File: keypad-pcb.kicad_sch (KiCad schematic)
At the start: 34 parts, among them J1 AVR-ISP-6, SW1 SW_Push, SW2 SW_Push, SW3 SW_Push, SW4 SW_Push, SW5 SW_Push, SW6 SW_Push, U1 ATmega32U4-A, Y1 Crystal_GND24_Small

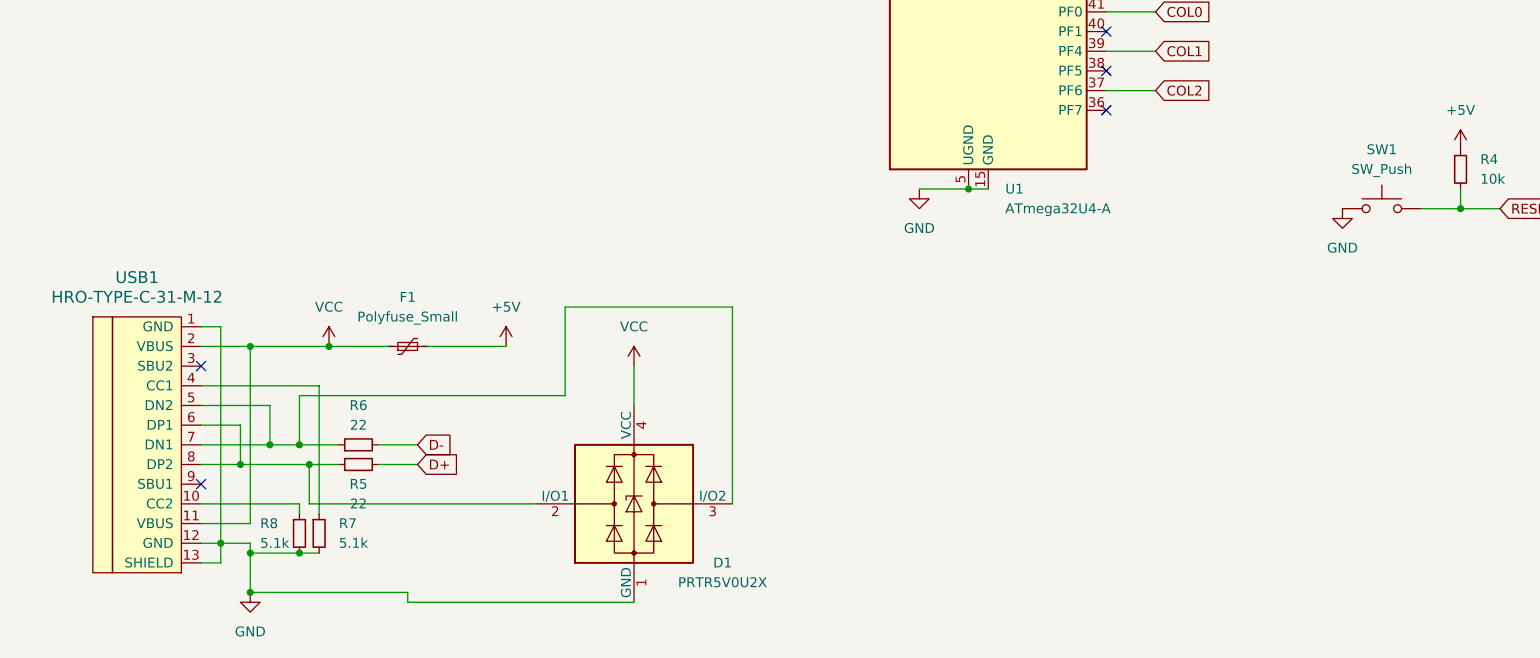
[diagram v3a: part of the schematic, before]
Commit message: power flag
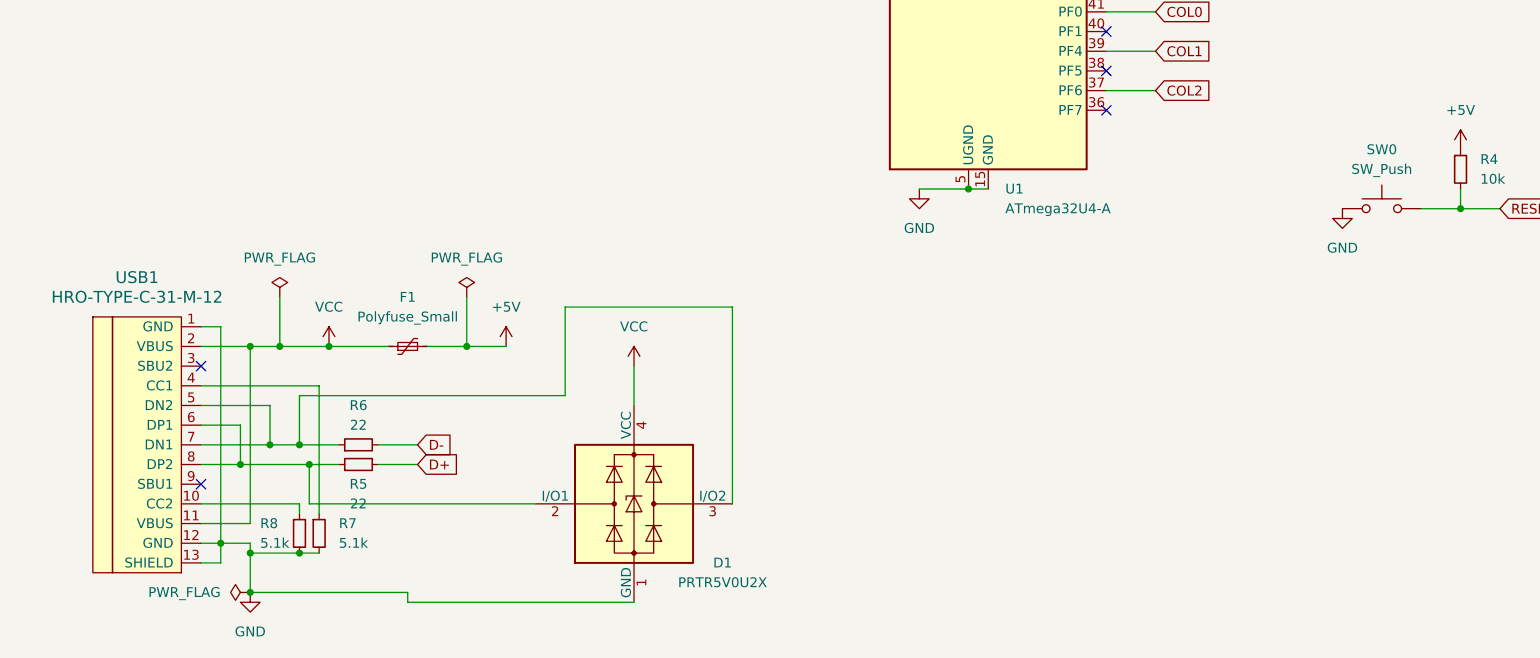
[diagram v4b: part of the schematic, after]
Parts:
- renumbered SW1 to SW0
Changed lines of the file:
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@@
   (junction (at 82.55 96.52) (diameter 0) (color 0 0 0 0)
   )
+  (junction (at 49.53 158.75) (diameter 0) (color 0 0 0 0)
+  )
   (junction (at 140.97 46.99) (diameter 0) (color 0 0 0 0)
   )
@@
   )
   (junction (at 73.66 91.44) (diameter 0) (color 0 0 0 0)
+  )
+  (junction (at 73.66 158.75) (diameter 0) (color 0 0 0 0)
   )
   (junction (at 52.07 171.45) (diameter 0) (color 0 0 0 0)
@@
     (stroke (width 0) (type default))
   )
-  (wire (pts (xy 68.58 158.75) (xy 78.74 158.75))
+  (wire (pts (xy 68.58 158.75) (xy 73.66 158.75))
     (stroke (width 0) (type default))
   )
@@
     (stroke (width 0) (type default))
   )
+  (wire (pts (xy 49.53 152.4) (xy 49.53 158.75))
+    (stroke (width 0) (type default))
+  )
   (wire (pts (xy 66.04 190.5) (xy 45.72 190.5))
     (stroke (width 0) (type default))
@@
     (stroke (width 0) (type default))
   )
+  (wire (pts (xy 49.53 158.75) (xy 55.88 158.75))
+    (stroke (width 0) (type default))
+  )
   (wire (pts (xy 52.07 185.42) (xy 54.61 185.42))
     (stroke (width 0) (type default))
@@
     (stroke (width 0) (type default))
   )
+  (wire (pts (xy 73.66 152.4) (xy 73.66 158.75))
+    (stroke (width 0) (type default))
+  )
   (wire (pts (xy 41.91 184.15) (xy 45.72 184.15))
     (stroke (width 0) (type default))
@@
     (stroke (width 0) (type default))
   )
-  (wire (pts (xy 45.72 158.75) (xy 55.88 158.75))
+  (wire (pts (xy 45.72 158.75) (xy 49.53 158.75))
     (stroke (width 0) (type default))
   )
@@
   )
   (wire (pts (xy 119.38 82.55) (xy 125.73 82.55))
+    (stroke (width 0) (type default))
+  )
+  (wire (pts (xy 73.66 158.75) (xy 78.74 158.75))
     (stroke (width 0) (type default))
   )
@@
     )
   )
+  (symbol (lib_id "power:PWR_FLAG") (at 45.72 190.5 90) (unit 1)
+    (in_bom yes) (on_board yes) (dnp no) (fields_autoplaced)
+    (property "Reference" "#FLG03" (at 43.815 190.5 0)
+      (effects (font (size 1.27 1.27)) hide)
+    )
+    (property "Value" "PWR_FLAG" (at 41.91 190.5 90)
+      (effects (font (size 1.27 1.27)) (justify left))
+    )
+    (property "Footprint" "" (at 45.72 190.5 0)
+      (effects (font (size 1.27 1.27)) hide)
+    )
+    (property "Datasheet" "~" (at 45.72 190.5 0)
+      (effects (font (size 1.27 1.27)) hide)
+    )
+    (pin "1")
+    (instances
+      (project "keypad-pcb"
+        (path "/73f1bcf6-a3cb-4955-8c73-ee07117345ce"
+          (reference "#FLG03") (unit 1)
+        )
+      )
+    )
+  )
   (symbol (lib_id "Device:C_Small") (at 64.77 93.98 0) (unit 1)
     (in_bom yes) (on_board yes) (dnp no) (fields_autoplaced)
@@
         (path "/73f1bcf6-a3cb-4955-8c73-ee07117345ce"
           (reference "#PWR012") (unit 1)
+        )
+      )
+    )
+  )
+  (symbol (lib_id "power:PWR_FLAG") (at 49.53 152.4 0) (unit 1)
+    (in_bom yes) (on_board yes) (dnp no) (fields_autoplaced)
+    (property "Reference" "#FLG01" (at 49.53 150.495 0)
+      (effects (font (size 1.27 1.27)) hide)
+    )
+    (property "Value" "PWR_FLAG" (at 49.53 147.32 0)
+      (effects (font (size 1.27 1.27)))
+    )
+    (property "Footprint" "" (at 49.53 152.4 0)
+      (effects (font (size 1.27 1.27)) hide)
+    )
+    (property "Datasheet" "~" (at 49.53 152.4 0)
+      (effects (font (size 1.27 1.27)) hide)
+    )
+    (pin "1")
+    (instances
+      (project "keypad-pcb"
+        (path "/73f1bcf6-a3cb-4955-8c73-ee07117345ce"
+          (reference "#FLG01") (unit 1)
+        )
+      )
+    )
+  )
+  (symbol (lib_id "power:PWR_FLAG") (at 73.66 152.4 0) (unit 1)
+    (in_bom yes) (on_board yes) (dnp no) (fields_autoplaced)
+    (property "Reference" "#FLG02" (at 73.66 150.495 0)
+      (effects (font (size 1.27 1.27)) hide)
+    )
+    (property "Value" "PWR_FLAG" (at 73.66 147.32 0)
+      (effects (font (size 1.27 1.27)))
+    )
+    (property "Footprint" "" (at 73.66 152.4 0)
+      (effects (font (size 1.27 1.27)) hide)
+    )
+    (property "Datasheet" "~" (at 73.66 152.4 0)
+      (effects (font (size 1.27 1.27)) hide)
+    )
+    (pin "1")
+    (instances
+      (project "keypad-pcb"
+        (path "/73f1bcf6-a3cb-4955-8c73-ee07117345ce"
+          (reference "#FLG02") (unit 1)
         )
       )
@@
   (symbol (lib_id "Switch:SW_Push") (at 191.77 140.97 0) (unit 1)
     (in_bom yes) (on_board yes) (dnp no) (fields_autoplaced)
-    (property "Reference" "SW1" (at 191.77 133.35 0)
+    (property "Reference" "SW0" (at 191.77 133.35 0)
       (effects (font (size 1.27 1.27)))
     )
@@
       (project "keypad-pcb"
         (path "/73f1bcf6-a3cb-4955-8c73-ee07117345ce"
-          (reference "SW1") (unit 1)
-        )
-      )
+          (reference "SW0") (unit 1)
+        )
+      )

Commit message: footprints
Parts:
- C1, C2, C3, C4, C5, C6, C7: footprint (none) -> Capacitor_SMD:C_0805_2012Metric
- D1: footprint Package_TO_SOT_SMD:SOT-143 -> random-keyboard-parts:SOT143B
- D2, D3, D4, D5, D6, D7: footprint (none) -> Diode_SMD:D_SOD-123
- F1: footprint (none) -> Fuse:Fuse_1206_3216Metric
- J1: footprint (none) -> random-keyboard-parts:Reset_Pretty-Mask
- R1, R2, R3, R4, R5, R6, R7, R8: footprint (none) -> Resistor_SMD:R_0805_2012Metric
- SW0: footprint (none) -> Button_Switch_SMD:SW_SPST_SKQG_WithStem
- SW1, SW2, SW3, SW4, SW5, SW6: footprint (none) -> marbastlib-mx:SW_MX_HS_1u
- USB1: footprint (none) -> Type-C:HRO-TYPE-C-31-M-12
- Y1: footprint (none) -> Crystal:Crystal_SMD_3225-4Pin_3.2x2.5mm
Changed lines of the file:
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@@
       (effects (font (size 1.27 1.27)) (justify left))
     )
-    (property "Footprint" "" (at 201.93 135.89 0)
+    (property "Footprint" "Resistor_SMD:R_0805_2012Metric" (at 201.93 135.89 0)
       (effects (font (size 1.27 1.27)) hide)
     )
@@
       (effects (font (size 1.27 1.27)) (justify right))
     )
-    (property "Footprint" "" (at 71.12 35.56 0)
+    (property "Footprint" "Diode_SMD:D_SOD-123" (at 71.12 35.56 0)
       (effects (font (size 1.27 1.27)) hide)
     )
@@
       (effects (font (size 1.27 1.27)))
     )
-    (property "Footprint" "" (at 40.64 45.72 0)
+    (property "Footprint" "marbastlib-mx:SW_MX_HS_1u" (at 40.64 45.72 0)
       (effects (font (size 1.27 1.27)) hide)
     )
@@
       (effects (font (size 1.27 1.27)))
     )
-    (property "Footprint" "" (at 59.69 173.99 0)
+    (property "Footprint" "Resistor_SMD:R_0805_2012Metric" (at 59.69 173.99 0)
       (effects (font (size 1.27 1.27)) hide)
     )
@@
       (effects (font (size 1.27 1.27)))
     )
-    (property "Footprint" "" (at 59.69 171.45 0)
+    (property "Footprint" "Resistor_SMD:R_0805_2012Metric" (at 59.69 171.45 0)
       (effects (font (size 1.27 1.27)) hide)
     )
@@
       (effects (font (size 1.27 1.27)) (justify right))
     )
-    (property "Footprint" "" (at 35.56 54.61 0)
+    (property "Footprint" "Diode_SMD:D_SOD-123" (at 35.56 54.61 0)
       (effects (font (size 1.27 1.27)) hide)
     )
@@
       (effects (font (size 1.27 1.27)) (justify left))
     )
-    (property "Footprint" "" (at 54.61 182.88 0)
+    (property "Footprint" "Resistor_SMD:R_0805_2012Metric" (at 54.61 182.88 0)
       (effects (font (size 1.27 1.27)) hide)
     )
@@
       (effects (font (size 1.27 1.27)))
     )
-    (property "Footprint" "" (at 116.84 85.09 0)
+    (property "Footprint" "Resistor_SMD:R_0805_2012Metric" (at 116.84 85.09 0)
       (effects (font (size 1.27 1.27)) hide)
     )
@@
       (effects (font (size 1.27 1.27)) (justify left))
     )
-    (property "Footprint" "" (at 52.07 182.88 0)
+    (property "Footprint" "Resistor_SMD:R_0805_2012Metric" (at 52.07 182.88 0)
       (effects (font (size 1.27 1.27)) hide)
     )
@@
       (effects (font (size 1.27 1.27)) (justify left))
     )
-    (property "Footprint" "" (at 55.88 93.98 0)
+    (property "Footprint" "Capacitor_SMD:C_0805_2012Metric" (at 55.88 93.98 0)
       (effects (font (size 1.27 1.27)) hide)
     )
@@
       (effects (font (size 1.27 1.27)))
     )
-    (property "Footprint" "" (at 58.42 26.67 0)
+    (property "Footprint" "marbastlib-mx:SW_MX_HS_1u" (at 58.42 26.67 0)
       (effects (font (size 1.27 1.27)) hide)
     )
@@
       (effects (font (size 1.27 1.27)))
     )
-    (property "Footprint" "" (at 40.64 26.67 0)
+    (property "Footprint" "marbastlib-mx:SW_MX_HS_1u" (at 40.64 26.67 0)
       (effects (font (size 1.27 1.27)) hide)
     )
@@
       (effects (font (size 1.27 1.27)) (justify left))
     )
-    (property "Footprint" "" (at 64.77 93.98 0)
+    (property "Footprint" "Capacitor_SMD:C_0805_2012Metric" (at 64.77 93.98 0)
       (effects (font (size 1.27 1.27)) hide)
     )
@@
       (effects (font (size 1.27 1.27)) (justify right))
     )
-    (property "Footprint" "" (at 53.34 35.56 0)
+    (property "Footprint" "Diode_SMD:D_SOD-123" (at 53.34 35.56 0)
       (effects (font (size 1.27 1.27)) hide)
     )
@@
       (effects (font (size 1.27 1.27)))
     )
-    (property "Footprint" "" (at 71.12 157.48 0)
+    (property "Footprint" "Fuse:Fuse_1206_3216Metric" (at 71.12 157.48 0)
       (effects (font (size 1.27 1.27)) (justify left) hide)
     )
@@
       (effects (font (size 1.27 1.27)))
     )
-    (property "Footprint" "" (at 58.42 45.72 0)
+    (property "Footprint" "marbastlib-mx:SW_MX_HS_1u" (at 58.42 45.72 0)
       (effects (font (size 1.27 1.27)) hide)
     )
@@
       (effects (font (size 1.27 1.27)))
     )
-    (property "Footprint" "Package_TO_SOT_SMD:SOT-143" (at 96.774 179.07 0)
+    (property "Footprint" "random-keyboard-parts:SOT143B" (at 96.774 179.07 0)
       (effects (font (size 1.27 1.27)) hide)
     )
@@
       (effects (font (size 1.27 1.27)))
     )
-    (property "Footprint" "" (at 116.84 76.2 0)
+    (property "Footprint" "Resistor_SMD:R_0805_2012Metric" (at 116.84 76.2 0)
       (effects (font (size 1.27 1.27)) hide)
     )
@@
       (effects (font (size 1.27 1.27)))
     )
-    (property "Footprint" "" (at 163.83 107.95 0)
+    (property "Footprint" "Resistor_SMD:R_0805_2012Metric" (at 163.83 107.95 0)
       (effects (font (size 1.27 1.27)) hide)
     )
@@
       (effects (font (size 1.27 1.27)) (justify left))
     )
-    (property "Footprint" "" (at 242.57 81.28 0)
+    (property "Footprint" "Capacitor_SMD:C_0805_2012Metric" (at 242.57 81.28 0)
       (effects (font (size 1.27 1.27)) hide)
     )
@@
       (effects (font (size 1.27 1.27)))
     )
-    (property "Footprint" "" (at 76.2 45.72 0)
+    (property "Footprint" "marbastlib-mx:SW_MX_HS_1u" (at 76.2 45.72 0)
       (effects (font (size 1.27 1.27)) hide)
     )
@@
       (effects (font (size 1.27 1.27)) (justify right))
     )
-    (property "Footprint" "" (at 53.34 54.61 0)
+    (property "Footprint" "Diode_SMD:D_SOD-123" (at 53.34 54.61 0)
       (effects (font (size 1.27 1.27)) hide)
     )
@@
       (effects (font (size 1.27 1.27)))
     )
-    (property "Footprint" "" (at 191.77 135.89 0)
+    (property "Footprint" "Button_Switch_SMD:SW_SPST_SKQG_WithStem" (at 191.77 135.89 0)
       (effects (font (size 1.27 1.27)) hide)
     )
@@
       (effects (font (size 1.27 1.27)) (justify left))
     )
-    (property "Footprint" "" (at 82.55 93.98 0)
+    (property "Footprint" "Capacitor_SMD:C_0805_2012Metric" (at 82.55 93.98 0)
       (effects (font (size 1.27 1.27)) hide)
     )
@@
       (effects (font (size 1.27 1.27)) (justify left))
     )
-    (property "Footprint" "" (at 217.17 81.28 0)
+    (property "Footprint" "Capacitor_SMD:C_0805_2012Metric" (at 217.17 81.28 0)
       (effects (font (size 1.27 1.27)) hide)
     )
@@
       (effects (font (size 1.27 1.27)) (justify left))
     )
-    (property "Footprint" "" (at 73.66 93.98 0)
+    (property "Footprint" "Capacitor_SMD:C_0805_2012Metric" (at 73.66 93.98 0)
       (effects (font (size 1.27 1.27)) hide)
     )
@@
       (effects (font (size 1.27 1.27)))
     )
-    (property "Footprint" "" (at 229.87 69.85 0)
+    (property "Footprint" "Crystal:Crystal_SMD_3225-4Pin_3.2x2.5mm" (at 229.87 69.85 0)
       (effects (font (size 1.27 1.27)) hide)
     )
@@
       (effects (font (size 1.27 1.27)) (justify right))
     )
-    (property "Footprint" "" (at 71.12 54.61 0)
+    (property "Footprint" "Diode_SMD:D_SOD-123" (at 71.12 54.61 0)
       (effects (font (size 1.27 1.27)) hide)
     )
@@
       (effects (font (size 1.524 1.524)))
     )
-    (property "Footprint" "" (at 36.83 170.18 0)
+    (property "Footprint" "Type-C:HRO-TYPE-C-31-M-12" (at 36.83 170.18 0)
       (effects (font (size 1.524 1.524)) hide)
     )
@@
       (effects (font (size 1.27 1.27)) (justify right))
     )
-    (property "Footprint" "" (at 35.56 35.56 0)
+    (property "Footprint" "Diode_SMD:D_SOD-123" (at 35.56 35.56 0)
       (effects (font (size 1.27 1.27)) hide)
     )
@@
       (effects (font (size 1.27 1.27)) (justify right))
     )
-    (property "Footprint" "" (at 223.52 120.65 90)
+    (property "Footprint" "random-keyboard-parts:Reset_Pretty-Mask" (at 223.52 120.65 90)
       (effects (font (size 1.27 1.27)) hide)
     )
@@
       (effects (font (size 1.27 1.27)))
     )
-    (property "Footprint" "" (at 76.2 26.67 0)
+    (property "Footprint" "marbastlib-mx:SW_MX_HS_1u" (at 76.2 26.67 0)
       (effects (font (size 1.27 1.27)) hide)
     )
@@
       (effects (font (size 1.27 1.27)) (justify right))
     )
-    (property "Footprint" "" (at 115.57 90.17 0)
-      (effects (font (size 1.27 1.27)) hide)
-    )
+    (property "Footprint" "Capacitor_SMD:C_0805_2012Metric" (at 115.57 90.17 0)
+      (effects (font (size 1.27 1.27)) hide)
+    )
